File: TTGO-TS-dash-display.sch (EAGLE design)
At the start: 35 parts, among them U8 NCP1117LPST50T3G

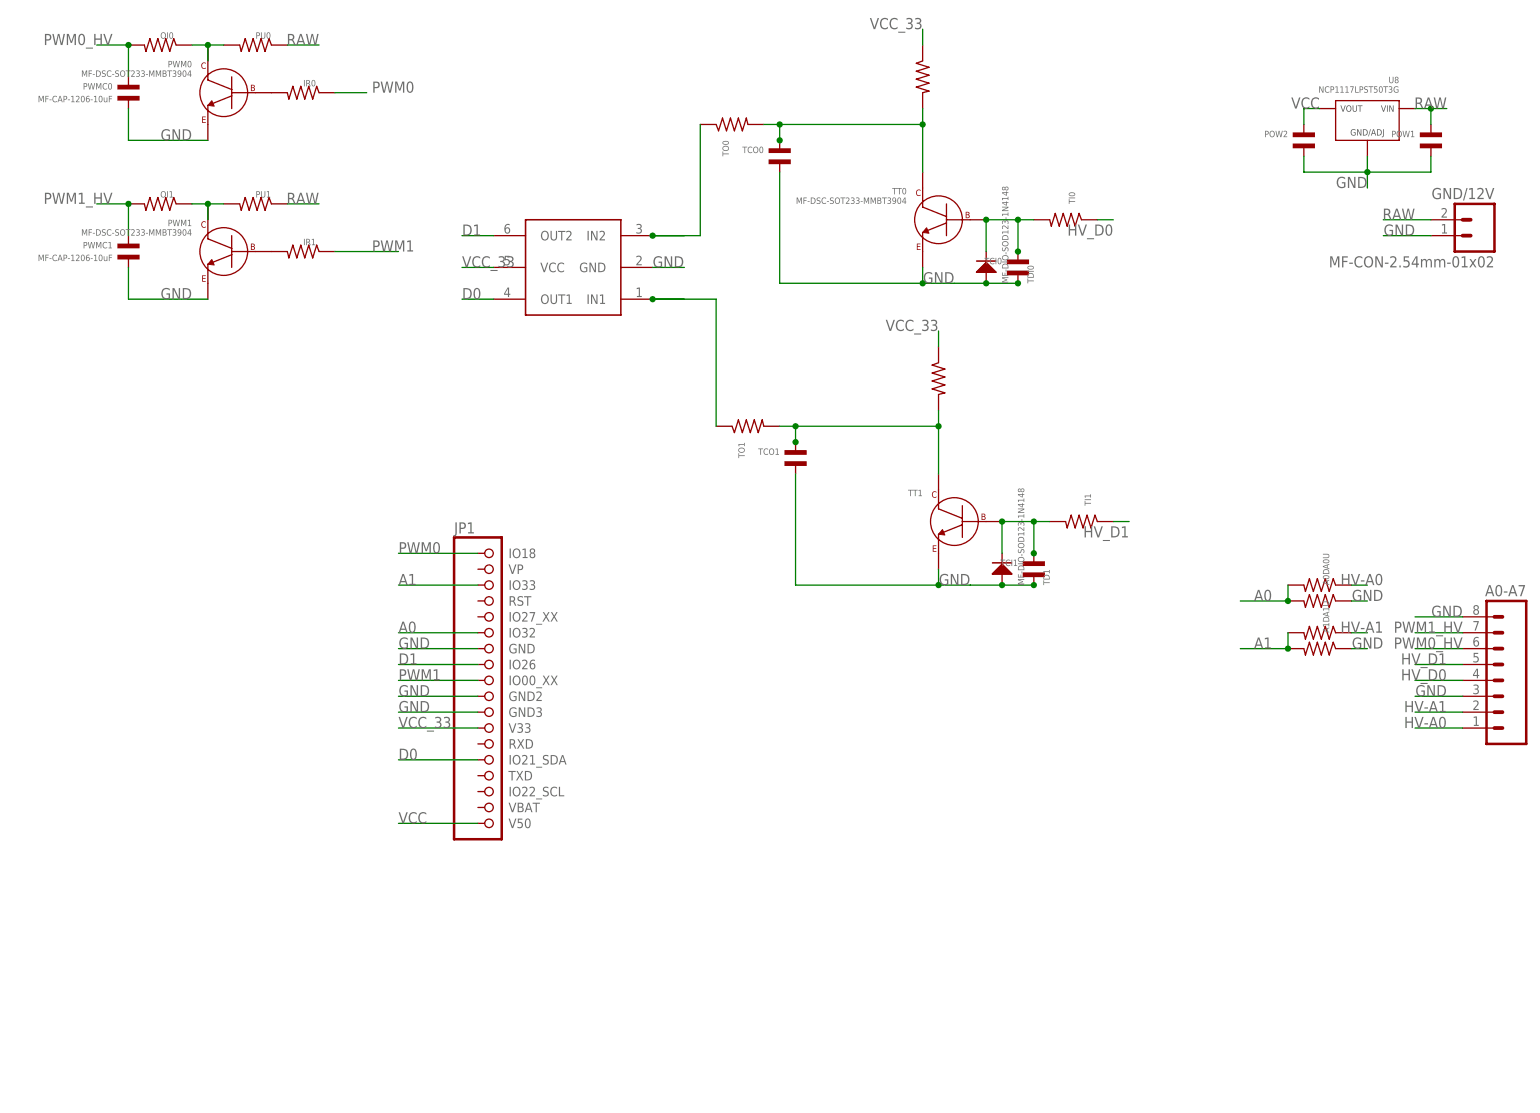
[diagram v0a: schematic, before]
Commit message: Tinkering with expected changes for dash-mount board
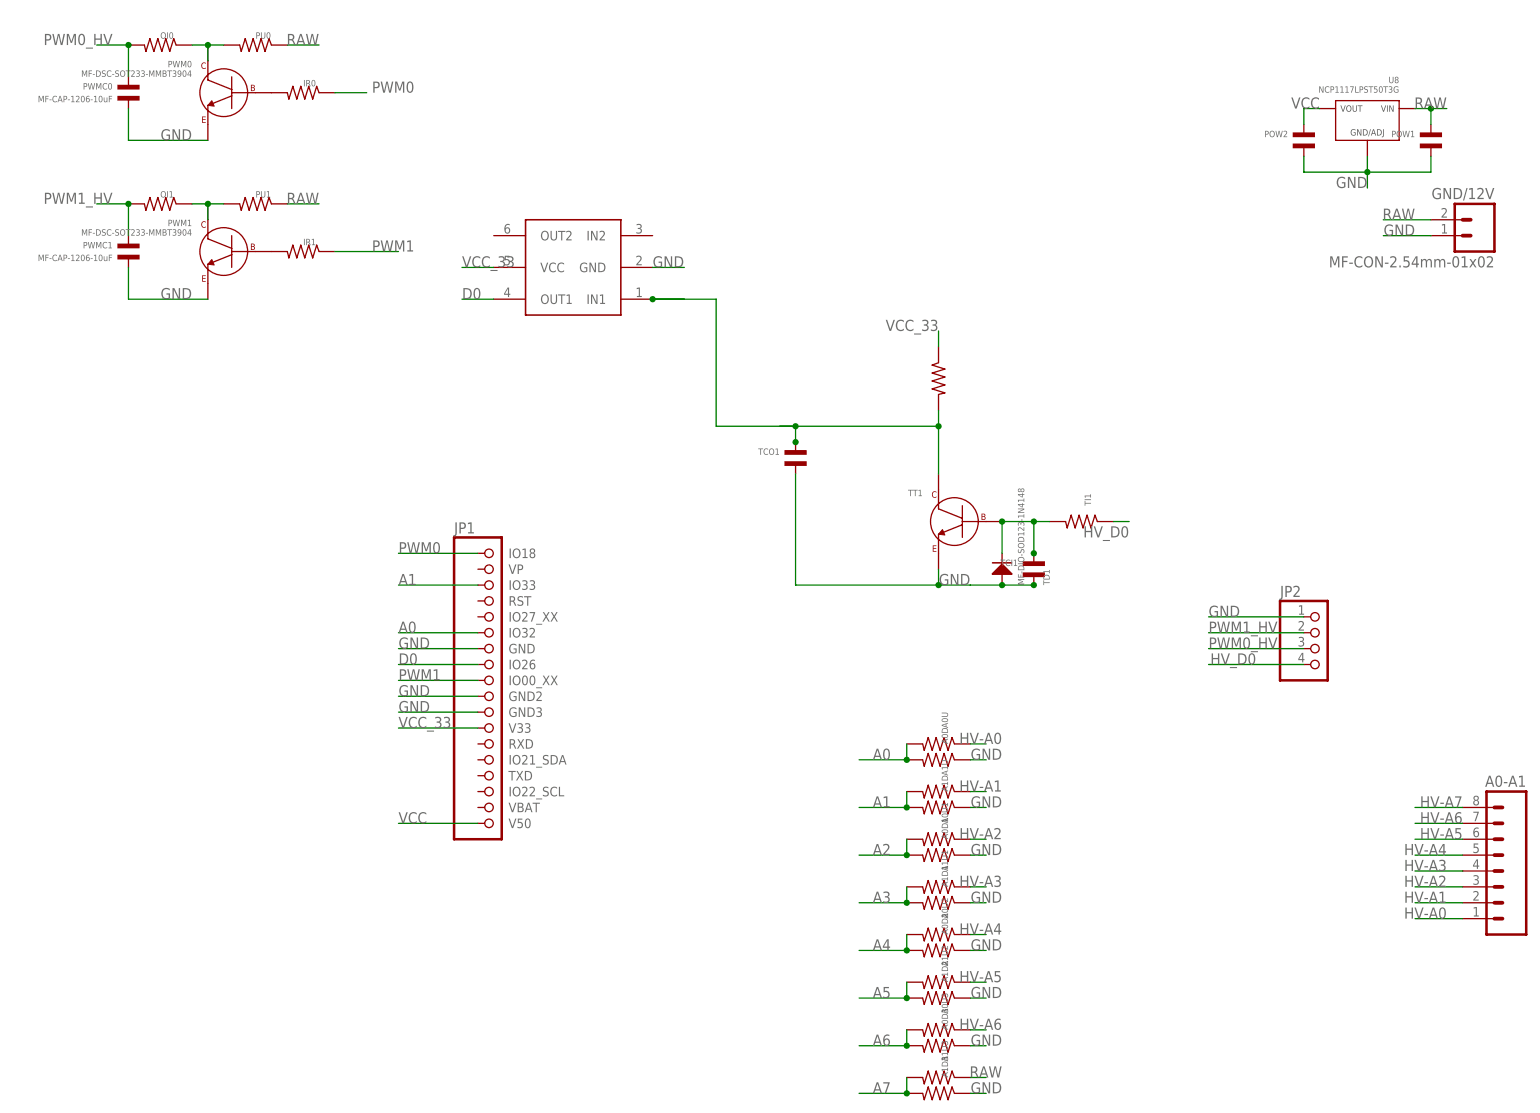
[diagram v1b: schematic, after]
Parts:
- removed A0-A7: MF-CON-2.54mm-01x08, SparkFun-Connectors:M081X08
- removed TCI0, TCO0: (no value), MF_Passives:CAPACITOR_NP_1210
- removed TDI0: MF-DIO-SOD123-1N4148, MF_Discrete_Semiconductor:DIODES_1N4148_SOD-123
- removed TI0, TO0, TO1, TU0: (no value), MF_Passives:RESISTOR_1206
- removed TT0: MF-DSC-SOT233-MMBT3904, MF_Discrete_Semiconductor:NPN_BJTMMBT3904_SOT-23-3
- added A0-A1: MF-CON-2.54mm-01x08, SparkFun-Connectors:M081X08
- added A0D1, A0D2, A0D3, A0U1, A0U2, A0U3, A1D1, A1D2, A1D3, A1U1, A1U2, A1U3: (no value), MF_Passives:RESISTOR_1206
- added JP2: (no value), 00jim:HEADER-1X4
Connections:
- removed net D1: JP1.IO26, U$1.OUT2
- removed net HV_D1: A0-A7.5, TI1.P$1
- removed net IO21_D4: TCO0.P$1, TO0.P$2, TT0.COLLECTOR, TU0.P$2
- removed net N$2: TCI0.P$1, TDI0.CATHODE, TI0.P$2, TT0.BASE
- removed net N$8: TO1.P$1, U$1.IN1
- removed net N$9: TO0.P$1, U$1.IN2
- new net A2: A0D1.P$2, A0U1.P$2
- new net A3: A1D1.P$2, A1U1.P$2
- new net A4: A0D2.P$2, A0U2.P$2
- new net A5: A1D2.P$2, A1U2.P$2
- new net A6: A0D3.P$2, A0U3.P$2
- new net A7: A1D3.P$2, A1U3.P$2
- new net HV-A2: A0-A1.3, A0U1.P$1
- new net HV-A3: A0-A1.4, A1U1.P$1
- new net HV-A4: A0-A1.5, A0U2.P$1
- new net HV-A5: A0-A1.6, A1U2.P$1
- new net HV-A6: A0-A1.7, A0U3.P$1
- new net HV-A7: A0-A1.8
- net D0: now also JP1.IO26; no longer JP1.IO21_SDA
- net GND: now also A0D1.P$1, A0D2.P$1, A0D3.P$1, A1D1.P$1, A1D2.P$1, A1D3.P$1, JP2.1; no longer A0-A7.3, A0-A7.8, TCI0.P$2, TCO0.P$2, TDI0.ANODE, TT0.EMITTER
- net HV-A0: now also A0-A1.1; no longer A0-A7.1
- net HV-A1: now also A0-A1.2; no longer A0-A7.2
- net HV_D0: now also JP2.4, TI1.P$1; no longer A0-A7.4, TI0.P$1
- net IO21_D1: now also U$1.IN1; no longer TO1.P$2
- net PWM0_HV: now also JP2.3; no longer A0-A7.6
- net PWM1_HV: now also JP2.2; no longer A0-A7.7
- net RAW: now also A1U3.P$1
- net VCC_33: no longer TU0.P$1
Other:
- moved on the sheet: A0D, A0U, A1D, A1U
